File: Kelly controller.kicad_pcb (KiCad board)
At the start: 2 copper layers, 65.4 x 54.3 mm, 16 parts, among them J1 Conn_01x06_Female, J2 Conn_01x06_Female, J4 Meter, J5 48V, J6 12V, J7 5V, SW1 FNR, SW2 Foot Switch, SW3 Brake, SW4 Power Switch

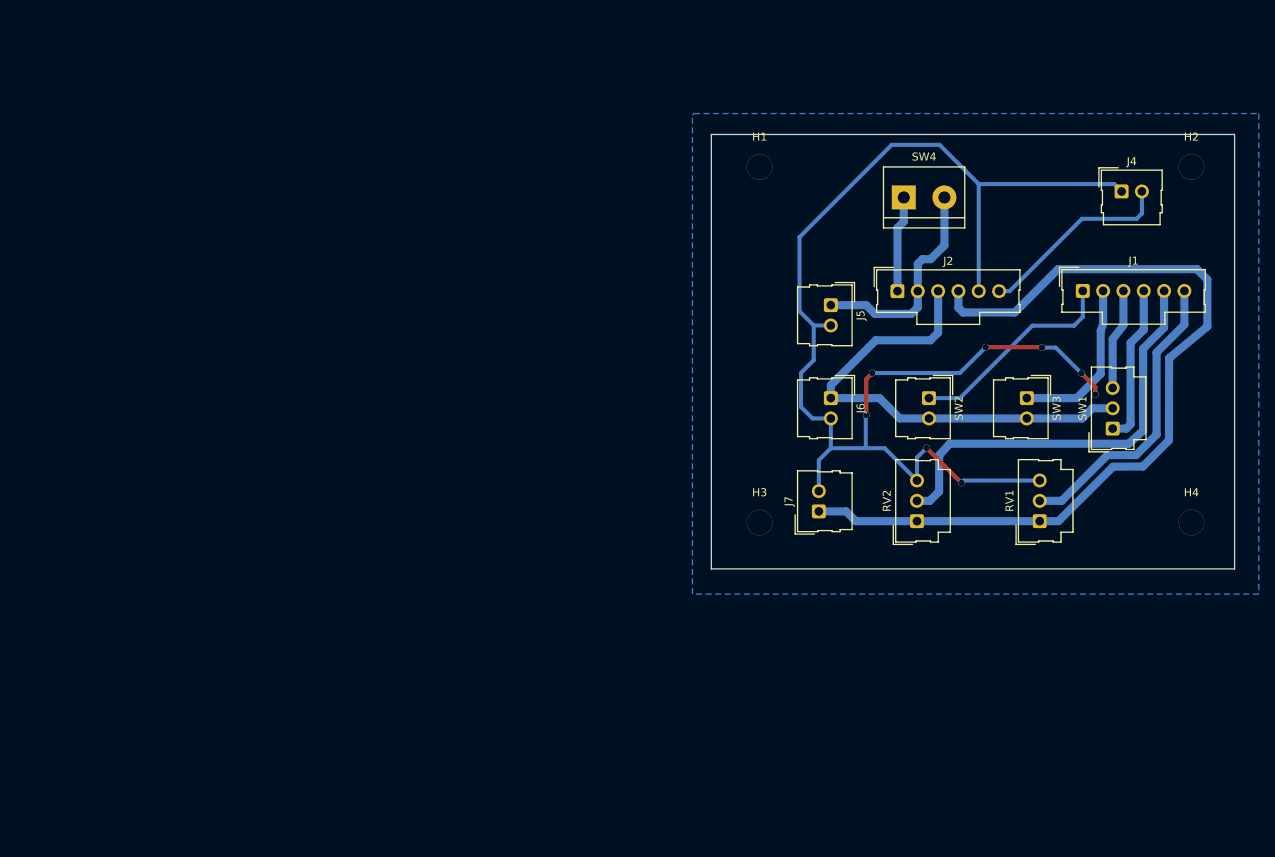
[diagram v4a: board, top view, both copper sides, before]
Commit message: redid board. vias were too small and close together. Also changed many pads to oval
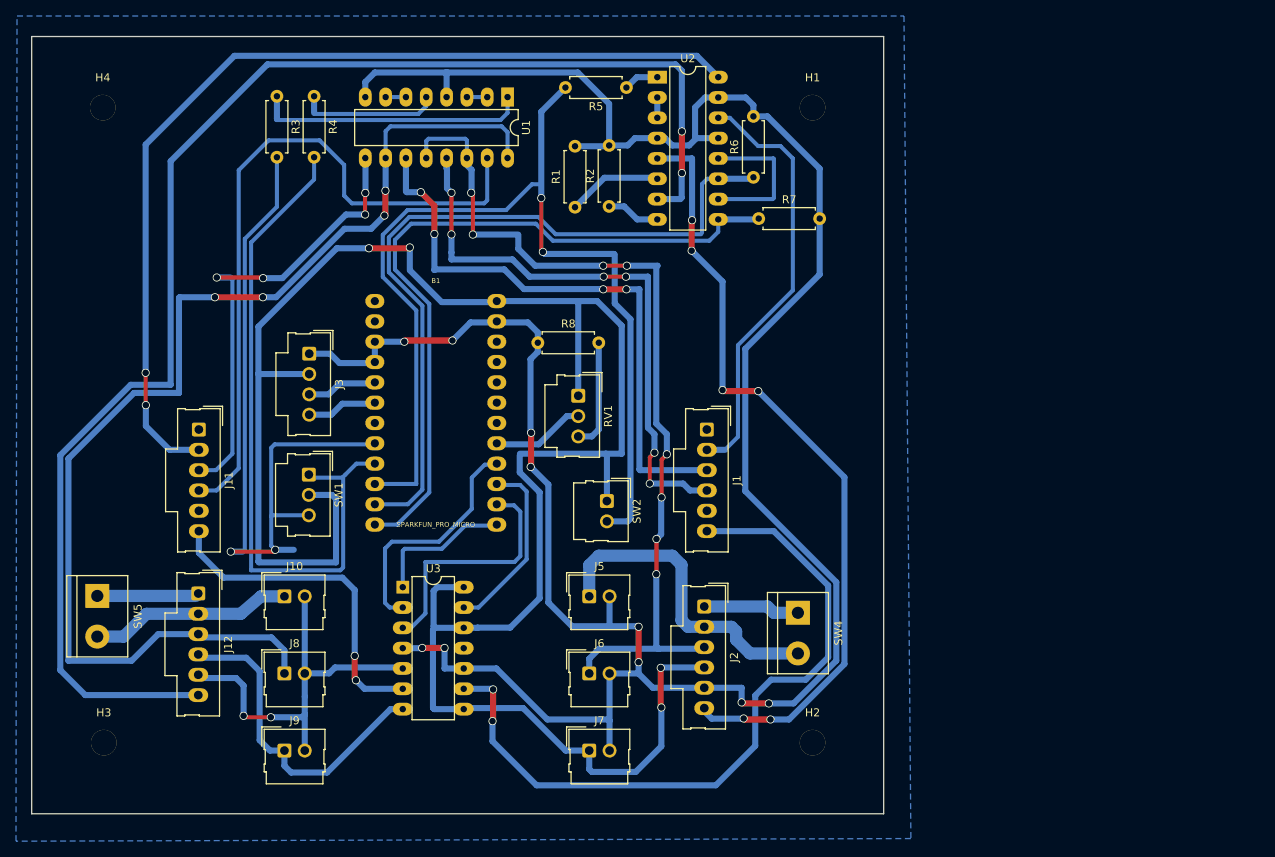
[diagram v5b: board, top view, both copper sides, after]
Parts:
- removed J4: Meter, Connector_Molex:Molex_SL_171971-0002_1x02_P2.54mm_Vertical
- removed RV2: Brake, Connector_Molex:Molex_SL_171971-0003_1x03_P2.54mm_Vertical
- removed SW3: Brake, Connector_Molex:Molex_SL_171971-0002_1x02_P2.54mm_Vertical
- added B1: SPARKFUN_PRO_MICRO, Boards:SPARKFUN_PRO_MICRO, F.Cu at (64.5, 78.2)
- added J10: 48V, Connector_Molex:Molex_SL_171971-0002_1x02_P2.54mm_Vertical, F.Cu at (45.6, 102.4)
- added J11: Conn_01x06_Female, Connector_Molex:Molex_SL_171971-0006_1x06_P2.54mm_Vertical, F.Cu at (34.9, 81.5)
- added J12: Conn_01x06_Female, Connector_Molex:Molex_SL_171971-0006_1x06_P2.54mm_Vertical, F.Cu at (34.8, 102.0)
- added J3: I2C throttle, Connector_Molex:Molex_SL_171971-0004_1x04_P2.54mm_Vertical, F.Cu at (48.7, 72.0)
- added J8: 12V, Connector_Molex:Molex_SL_171971-0002_1x02_P2.54mm_Vertical, F.Cu at (45.6, 112.0)
- added J9: 5V, Connector_Molex:Molex_SL_171971-0002_1x02_P2.54mm_Vertical, F.Cu at (45.6, 121.6)
- added R1: 1k, Resistor_THT:R_Axial_DIN0207_L6.3mm_D2.5mm_P7.62mm_Horizontal, F.Cu at (81.9, 53.7)
- added R2: 1k, Resistor_THT:R_Axial_DIN0207_L6.3mm_D2.5mm_P7.62mm_Horizontal, F.Cu at (86.2, 53.6)
- added R3: 220, Resistor_THT:R_Axial_DIN0207_L6.3mm_D2.5mm_P7.62mm_Horizontal, F.Cu at (44.7, 39.9)
- added R4: 220, Resistor_THT:R_Axial_DIN0207_L6.3mm_D2.5mm_P7.62mm_Horizontal, F.Cu at (49.3, 39.9)
- added R5: 220, Resistor_THT:R_Axial_DIN0207_L6.3mm_D2.5mm_P7.62mm_Horizontal, F.Cu at (88.3, 38.8)
- added R6: 10k, Resistor_THT:R_Axial_DIN0207_L6.3mm_D2.5mm_P7.62mm_Horizontal, F.Cu at (104.2, 50.0)
- added R7: 10k, Resistor_THT:R_Axial_DIN0207_L6.3mm_D2.5mm_P7.62mm_Horizontal, F.Cu at (104.9, 55.1)
- added R8: 1k, Resistor_THT:R_Axial_DIN0207_L6.3mm_D2.5mm_P7.62mm_Horizontal, F.Cu at (77.3, 70.7)
- added SW5: Power Switch, TerminalBlock:TerminalBlock_bornier-2_P5.08mm, F.Cu at (22.2, 102.3)
- added U1: LTV-247, Package_DIP:DIP-16_W7.62mm_LongPads, F.Cu at (73.5, 40.0)
- added U2: LTV-247, Package_DIP:DIP-16_W7.62mm_LongPads, F.Cu at (92.2, 37.5)
- added U3: MCP4251-xxxx-P, Package_DIP:DIP-14_W7.62mm, F.Cu at (60.4, 101.2)
- SW2: value Foot Switch -> SW_Push
- moved H4 145.6 mm to (22.9, 41.3)
- moved SW1 100.6 mm to (48.6, 87.1), turned to 270 degrees
- moved H3 86.5 mm to (23.0, 120.7)
- moved H2 86.2 mm to (111.6, 120.7)
- moved RV1 59.8 mm to (82.3, 77.3), turned to 270 degrees
- moved SW4 53.6 mm to (109.8, 104.4), turned to 270 degrees
- moved J1 50.1 mm to (98.4, 81.5), turned to 270 degrees
- moved J5 47.3 mm to (83.7, 102.4), turned to 0 degrees
- moved J2 46.2 mm to (98.1, 103.6), turned to 270 degrees
- moved J6 45.8 mm to (83.7, 112.0), turned to 0 degrees
- moved SW2 42.3 mm to (85.9, 90.4)
- moved J7 41.4 mm to (83.7, 121.6), turned to 0 degrees
- moved H1 9.93 mm to (111.6, 41.3)
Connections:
- RV1 pad 2: /Throttle -> Net-(B1-Pad17)
- RV1 pad 3: GND -> Net-(R8-Pad2)
- SW1 pad 1: /FWD -> /6-Reverse
- SW1 pad 2: 12V -> 5V
- SW1 pad 3: /REV -> /5-Forward
- SW2 pad 1: /Foot_SW -> 5V
- SW2 pad 2: 12V -> /10-CS
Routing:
- net /Meter-A: track 0.00 -> 179.0 mm, vias 0 -> 2
- net 5V: track 107.0 -> 261.4 mm, vias 0 -> 4
- net +12VA: track 0.00 -> 146.0 mm, vias 0 -> 4
- net GND: track 174.7 -> 320.4 mm, vias 8 -> 10
- net /10-CS: track 0.00 -> 128.4 mm, vias 0 -> 2
- net /Brake-A: track 0.00 -> 120.3 mm, vias 0 -> 2
- net /8-Meter: track 0.00 -> 94.0 mm
- net /5-Forward: track 0.00 -> 91.2 mm, vias 0 -> 2
- net /9-Meter: track 0.00 -> 91.1 mm
- net /6-Reverse: track 0.00 -> 87.0 mm
- net /FWD-A: track 0.00 -> 86.9 mm
- net /Meter: track 24.6 -> 99.2 mm, vias 0 -> 6
- net /REV: track 12.6 -> 74.2 mm, vias 0 -> 4
- net /REV-A: track 0.00 -> 57.8 mm, vias 0 -> 4
- net /Throttle: track 37.4 -> 91.7 mm, vias 0 -> 2
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- added copper zone on B.Cu, net (none)
- removed copper zone on B.Cu, net GND
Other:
- board size 65.4 x 54.3 mm -> 106.5 x 97.2 mm

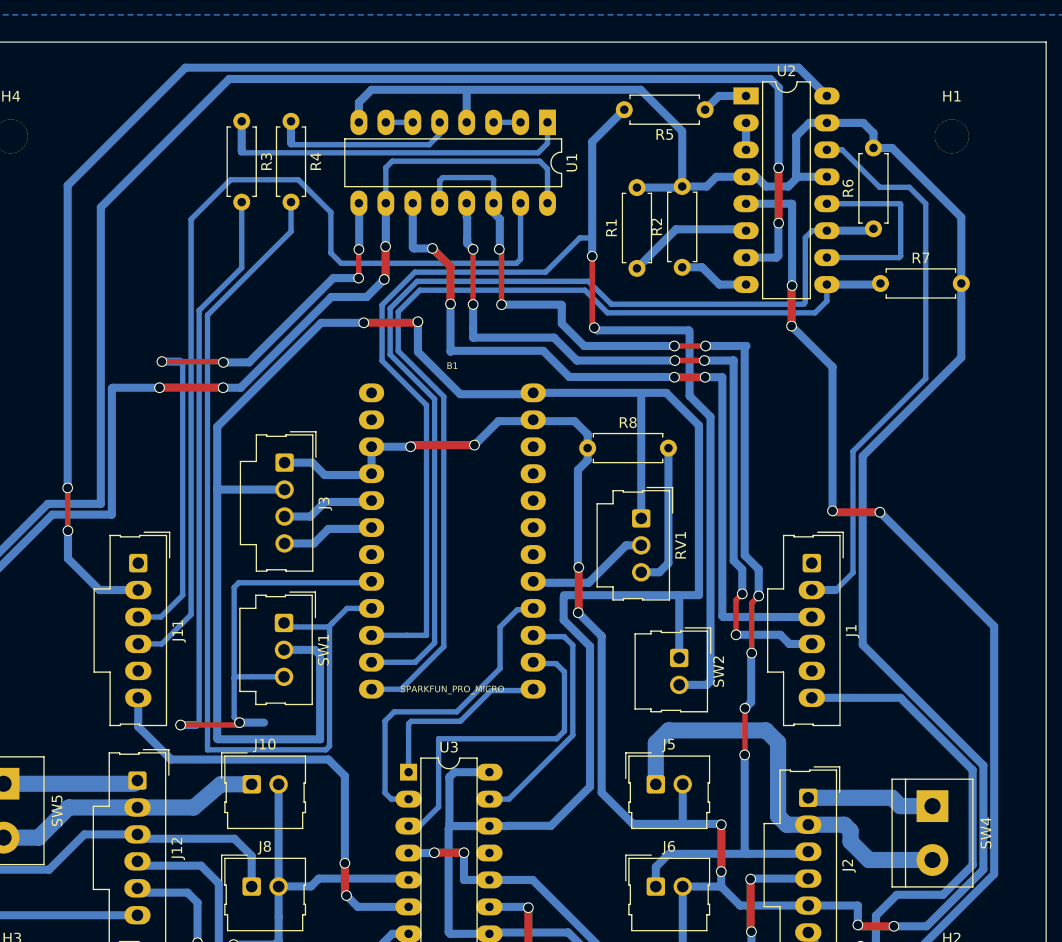
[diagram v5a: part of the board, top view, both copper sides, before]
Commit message: Cut first attempt at twin motor arduino board. During assembly had several lifted pads - need to use wider traces where practical. Brake lines were wired wrong. See notes in this commit for history. Next version will update traces, drop 5/12/48 v headers, fix brake line and add numerous test points to make testing and future modifications easier.
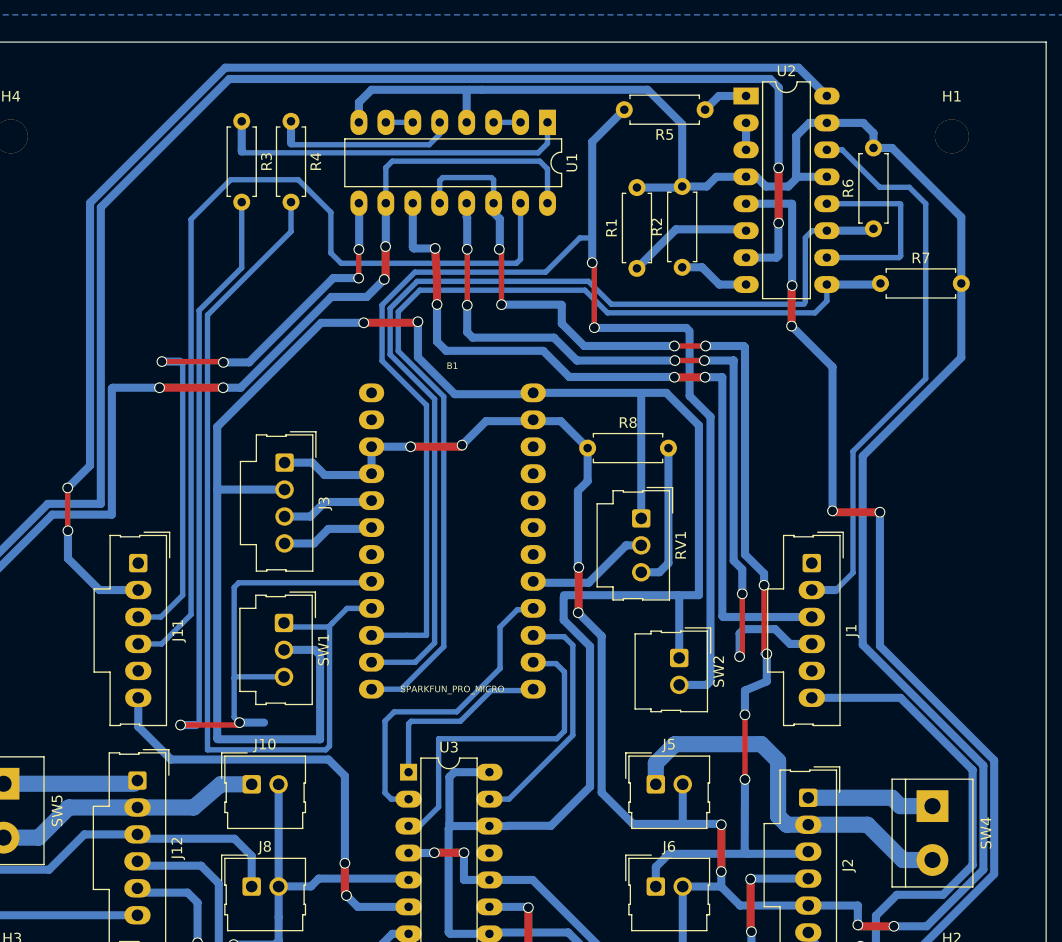
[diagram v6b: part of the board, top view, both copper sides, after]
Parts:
- SW2: value SW_Push -> Brake_SW
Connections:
- net Net-(B1-Pad5) renamed /SDA
- net Net-(B1-Pad6) renamed /SCL
- B1 pad 10: /10-CS -> /7-Brake
- B1 pad 13: Net-(B1-Pad13) -> /10-CS
- R5 pad 2: /10-CS -> /7-Brake
- SW2 pad 2: /10-CS -> /7-Brake
- U3 pad 1: Net-(B1-Pad13) -> /10-CS
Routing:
- net /7-Brake: track 0.00 -> 128.4 mm, vias 0 -> 2
- net /10-CS: track 128.4 -> 17.3 mm, vias 2 -> 0
- net Net-(B1-Pad13): track 17.3 -> 0.00 mm
- net /FWD: track 72.3 -> 76.5 mm
- net +48V: track 40.2 -> 36.4 mm
- net /Brake-A: track 120.3 -> 118.1 mm
- net 12V: track 111.2 -> 112.4 mm
